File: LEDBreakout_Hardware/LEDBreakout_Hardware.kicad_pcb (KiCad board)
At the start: 2 copper layers, 42.7 x 25.9 mm, 19 parts

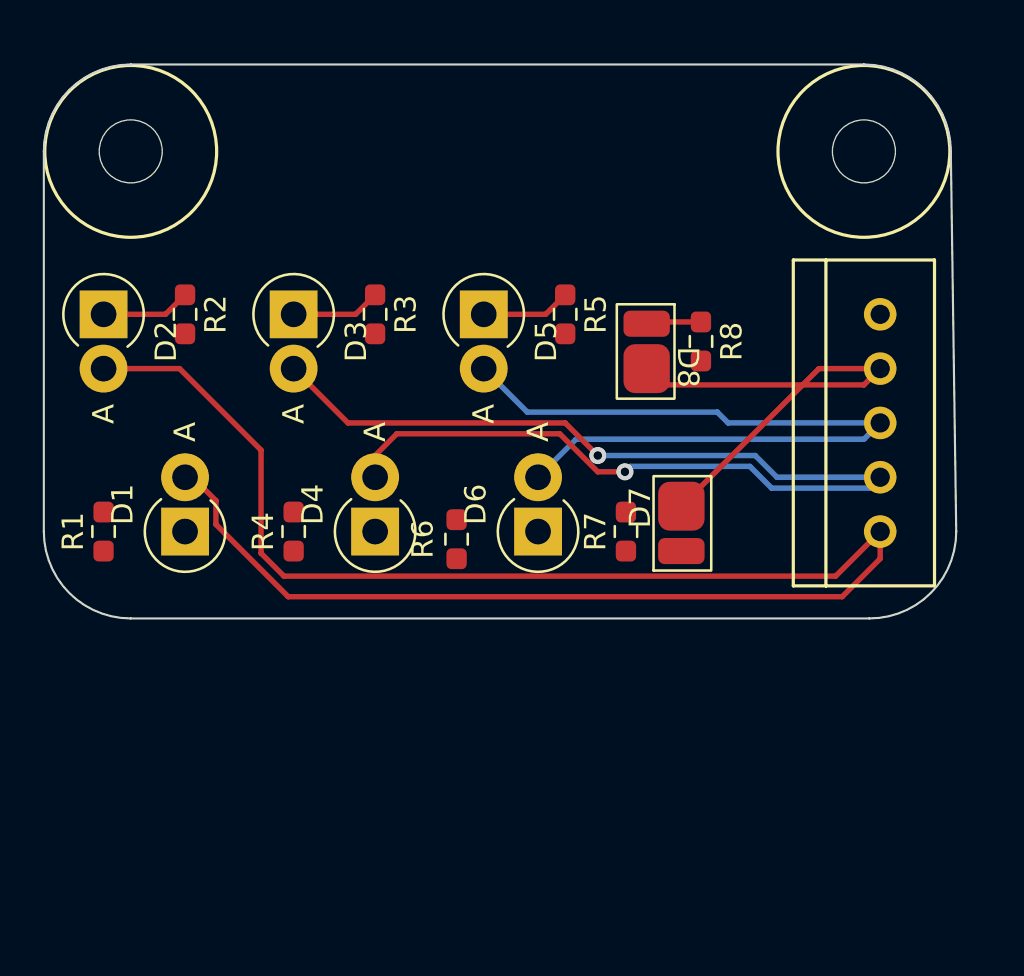
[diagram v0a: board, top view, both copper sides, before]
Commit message: Added 5V to LED connectors
Also added FETs to LEDs on breakout.
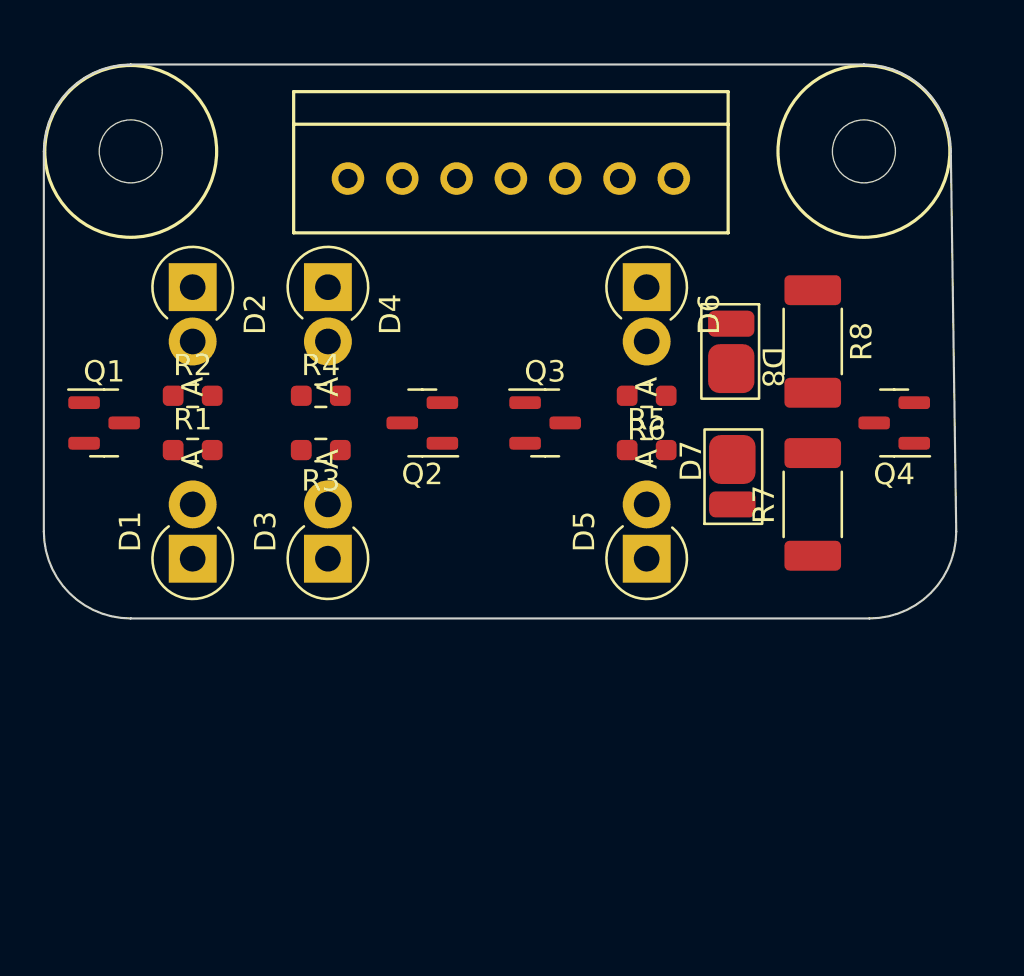
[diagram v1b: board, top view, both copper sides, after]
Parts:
- added Q1: BSS138, Package_TO_SOT_SMD:SOT-23, F.Cu at (64.8, 76.2)
- added Q2: BSS138, Package_TO_SOT_SMD:SOT-23, F.Cu at (79.7, 76.2)
- added Q3: BSS138, Package_TO_SOT_SMD:SOT-23, F.Cu at (85.4, 76.2)
- added Q4: BSS138, Package_TO_SOT_SMD:SOT-23, F.Cu at (101.7, 76.2)
- Conn1: value Molex_SL_05 -> Molex_SL_07; footprint MRDT_Connectors:MOLEX_SL_05_Vertical -> MRDT_Connectors:MOLEX_SL_07_Vertical
- R1, R2: value 90 Ω -> 88.7 Ω
- R3, R4: value 80 Ω -> 78.7 Ω
- R5, R6: value 57 Ω -> 82.5 Ω
- R7, R8: value 10 Ω -> 8 Ω; footprint Resistor_SMD:R_0603_1608Metric_Pad0.98x0.95mm_HandSolder -> Resistor_SMD:R_2010_5025Metric_Pad1.40x2.65mm_HandSolder
- moved Conn1 29.9 mm to (76.2, 64.8), turned to 0 degrees
- moved D5 13.7 mm to (90.2, 82.5), turned to 90 degrees
- moved D6 12.5 mm to (90.2, 69.8), turned to -90 degrees
- moved D4 11.6 mm to (75.3, 69.8), turned to -90 degrees
- moved D3 11.5 mm to (75.3, 82.5), turned to 90 degrees
- moved R6 11.1 mm to (90.2, 74.9), turned to 180 degrees
- moved R7 8.83 mm to (97.9, 80.0)
- moved R5 7.41 mm to (90.2, 77.5), turned to 0 degrees
- moved R3 6.84 mm to (74.9, 77.5), turned to 180 degrees
- moved R4 6.48 mm to (74.9, 74.9), turned to 0 degrees
- moved R1 5.65 mm to (68.9, 77.5), turned to 0 degrees
- moved R8 5.23 mm to (97.9, 72.4)
- moved D2 4.36 mm to (68.9, 69.8)
- moved D8 3.96 mm to (94.2, 72.5)
- moved R2 3.83 mm to (68.9, 74.9), turned to 0 degrees
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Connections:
- Conn1 pad 1: Net-(D1-A) -> 530nm
- Conn1 pad 2: Net-(D3-A) -> 522nm
- Conn1 pad 3: Net-(D5-A) -> 465nm
- Conn1 pad 4: Net-(D7-A) -> 400nm
- Conn1 pad 5: GND -> +5V
- D2 pad 1: Net-(D2-K) -> Net-(D1-K)
- D2 pad 2: Net-(D1-A) -> Net-(D2-A)
- D4 pad 1: Net-(D4-K) -> Net-(D3-K)
- D4 pad 2: Net-(D3-A) -> Net-(D4-A)
- D6 pad 1: Net-(D6-K) -> Net-(D5-K)
- D6 pad 2: Net-(D5-A) -> Net-(D6-A)
- D8 pad 1: Net-(D8-K) -> Net-(D7-K)
- D8 pad 2: Net-(D7-A) -> Net-(D8-A)
- R1 pad 1: Net-(D1-K) -> +5V
- R1 pad 2: GND -> Net-(D1-A)
- R2 pad 1: Net-(D2-K) -> +5V
- R2 pad 2: GND -> Net-(D2-A)
- R3 pad 1: Net-(D3-K) -> +5V
- R3 pad 2: GND -> Net-(D3-A)
- R4 pad 1: Net-(D4-K) -> +5V
- R4 pad 2: GND -> Net-(D4-A)
- R5 pad 1: Net-(D5-K) -> +5V
- R5 pad 2: GND -> Net-(D5-A)
- R6 pad 1: Net-(D6-K) -> +5V
- R6 pad 2: GND -> Net-(D6-A)
- R7 pad 1: Net-(D7-K) -> +5V
- R7 pad 2: GND -> Net-(D7-A)
- R8 pad 1: Net-(D8-K) -> +5V
- R8 pad 2: GND -> Net-(D8-A)
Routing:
- net Net-(D1-A): track 81.8 -> 0.00 mm
- net Net-(D3-A): track 56.1 -> 0.00 mm, vias 2 -> 0
- net Net-(D5-A): track 36.6 -> 0.00 mm
- net Net-(D7-A): track 23.5 -> 0.00 mm
- net Net-(D5-K): track 4.19 -> 0.00 mm
- net Net-(D3-K): track 4.19 -> 0.00 mm
- net Net-(D2-K): track 4.19 -> 0.00 mm
- net Net-(D8-K): track 2.57 -> 0.00 mm

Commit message: Added Traces for LED Breakout
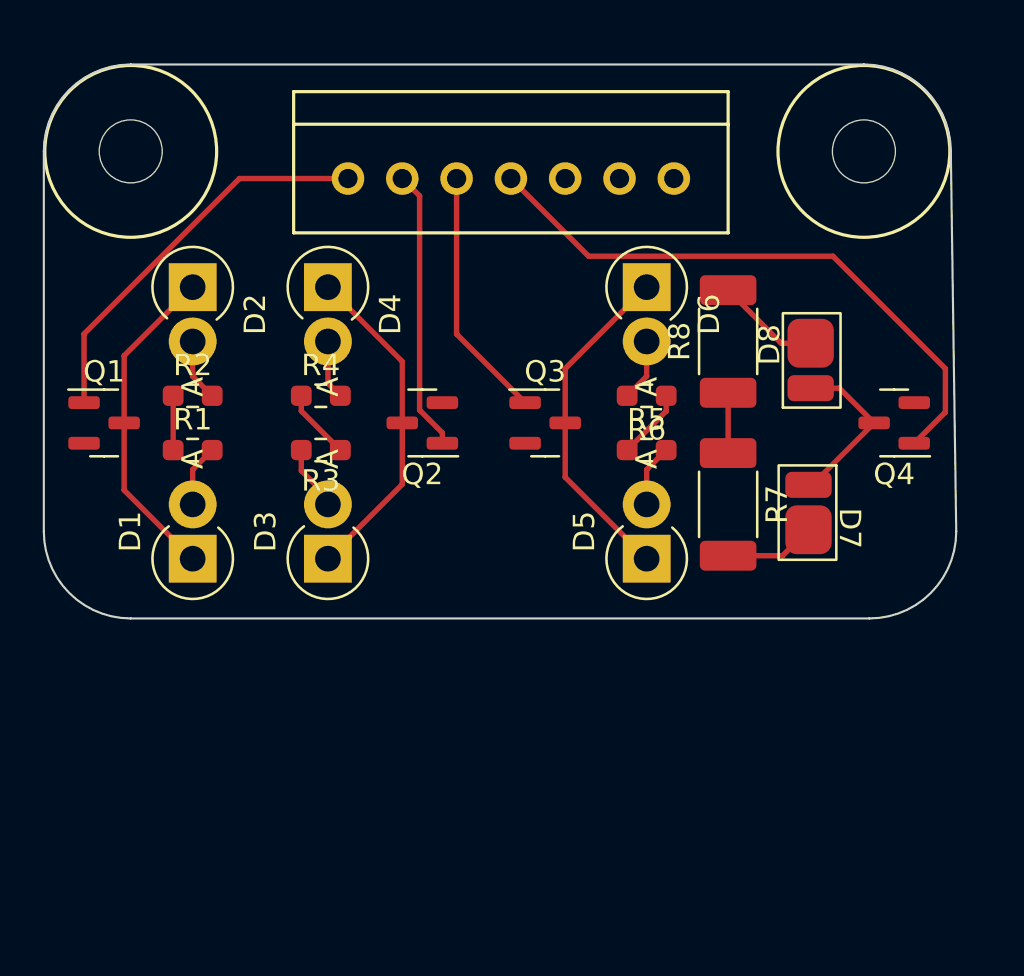
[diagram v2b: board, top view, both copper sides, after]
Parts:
- moved R7 3.96 mm to (94.0, 80.0), turned to -90 degrees
- moved R8 3.96 mm to (94.0, 72.4), turned to 90 degrees
- moved D8 3.80 mm to (97.8, 73.7), turned to 90 degrees
- moved D7 3.78 mm to (97.8, 80.0), turned to -90 degrees
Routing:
- net 400nm: track 0.00 -> 28.1 mm
- net 530nm: track 0.00 -> 18.6 mm
- net Net-(D3-K): track 0.00 -> 16.1 mm
- net Net-(D5-K): track 0.00 -> 15.9 mm
- net Net-(D1-K): track 0.00 -> 15.4 mm
- net 522nm: track 0.00 -> 13.2 mm
- net +5V: track 0.00 -> 12.0 mm
- net 465nm: track 0.00 -> 11.8 mm
- net Net-(D7-K): track 0.00 -> 7.91 mm
- net Net-(D8-A): track 0.00 -> 4.89 mm
- net Net-(D7-A): track 0.00 -> 4.26 mm
- net Net-(D3-A): track 0.00 -> 3.06 mm
- net Net-(D6-A): track 0.00 -> 2.92 mm
- net Net-(D5-A): track 0.00 -> 2.92 mm
- net Net-(D1-A): track 0.00 -> 2.92 mm
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
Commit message: Changes made based on layout review notes
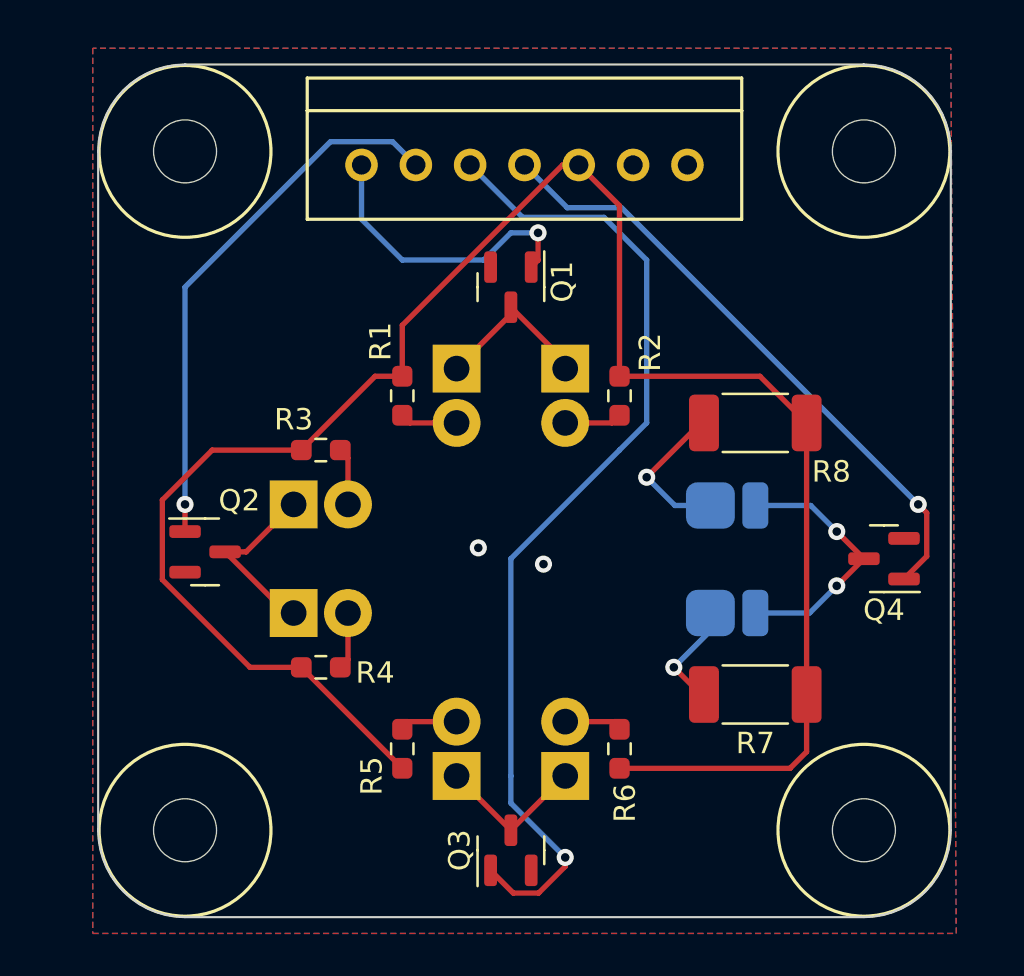
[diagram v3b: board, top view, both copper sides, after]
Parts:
- added REF**: 4_40_Hole, MRDT_Drill_Holes:4_40_Hole, F.Cu at (100.3, 95.2)
- added REF**: 4_40_Hole, MRDT_Drill_Holes:4_40_Hole, F.Cu at (68.6, 95.2)
- D1, D2, D3, D4, D5, D6, D7, D8: moved to B.Cu
- moved D6 23.2 mm to (86.4, 92.7), turned to 90 degrees
- moved Q1 20.1 mm to (83.8, 69.8), turned to -90 degrees
- moved Q3 20.1 mm to (83.8, 96.2), turned to 90 degrees
- moved R2 20.0 mm to (88.9, 74.9), turned to -90 degrees
- moved R5 18.1 mm to (78.7, 91.4), turned to 90 degrees
- moved D2 17.8 mm to (86.4, 73.7)
- moved R6 16.6 mm to (88.9, 91.4), turned to 90 degrees
- moved D4 15.3 mm to (73.7, 85.1), turned to 0 degrees
- moved D1 15.2 mm to (81.3, 73.7), turned to -90 degrees
- moved D5 13.5 mm to (81.3, 92.7)
- moved R4 12.7 mm to (74.9, 87.6)
- moved Q2 11.8 mm to (69.5, 82.2), turned to 0 degrees
- moved R1 10.1 mm to (78.7, 74.9), turned to -90 degrees
- moved R7 8.98 mm to (95.2, 88.9), turned to 180 degrees
- moved D8 7.23 mm to (94.3, 80.0), turned to 180 degrees
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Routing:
- net +5V: track 12.0 -> 90.7 mm
- net 465nm: track 11.8 -> 46.6 mm, vias 0 -> 1
- net 522nm: track 13.2 -> 25.5 mm, vias 0 -> 1
- net Net-(D5-K): track 15.9 -> 7.18 mm
- net Net-(D3-K): track 16.1 -> 8.51 mm
- net Net-(D1-K): track 15.4 -> 7.85 mm
- net 530nm: track 18.6 -> 13.8 mm, vias 0 -> 1
- net Net-(D7-K): track 7.91 -> 12.2 mm, vias 0 -> 2
- net Net-(D8-A): track 4.89 -> 7.26 mm, vias 0 -> 1
- net 400nm: track 28.1 -> 29.1 mm, vias 0 -> 1
- net Net-(D7-A): track 4.26 -> 5.18 mm, vias 0 -> 1
- net GND: vias 0 -> 2
- added copper zone on B.Cu, net GND
- added copper zone on F.Cu, net GND
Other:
- board size 42.7 x 25.9 mm -> 39.9 x 39.9 mm

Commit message: Added Pull Down Resistors to MOSFETs
And some other things
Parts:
- added R10: 4.7k Ω, Resistor_SMD:R_0603_1608Metric_Pad0.98x0.95mm_HandSolder, F.Cu at (67.8, 72.1)
- added R11: 4.7k Ω, Resistor_SMD:R_0603_1608Metric_Pad0.98x0.95mm_HandSolder, F.Cu at (67.8, 74.4)
- added R12: 4.7k Ω, Resistor_SMD:R_0603_1608Metric_Pad0.98x0.95mm_HandSolder, F.Cu at (67.8, 76.7)
- added R9: 4.7k Ω, Resistor_SMD:R_0603_1608Metric_Pad0.98x0.95mm_HandSolder, F.Cu at (67.8, 69.6)
- moved Q1 14.7 mm to (94.3, 80.2), turned to 180 degrees
- moved R1 10.5 mm to (89.1, 73.2), turned to 180 degrees
- moved Q4 6.59 mm to (96.5, 87.1)
- moved D3 6.12 mm to (79.8, 79.5), turned to 180 degrees
- moved R8 6.02 mm to (98.0, 81.5), turned to -90 degrees
- moved D2 5.99 mm to (89.9, 78.5), turned to 90 degrees
- moved D7 5.04 mm to (90.8, 88.6)
- moved D1 5.03 mm to (84.8, 77.2), turned to 90 degrees
- moved R2 4.75 mm to (93.5, 76.2), turned to 90 degrees
- moved Q2 4.66 mm to (73.5, 79.8), turned to -90 degrees
- moved D4 4.13 mm to (77.7, 84.3), turned to 180 degrees
- moved D5 3.78 mm to (80.0, 89.2), turned to -90 degrees
- moved D8 3.77 mm to (93.1, 83.6)
- moved R7 3.66 mm to (93.2, 91.9)
- moved R4 3.61 mm to (72.6, 84.8), turned to -90 degrees
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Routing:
- net +5V: track 90.7 -> 0.00 mm
- net 465nm: track 46.6 -> 0.00 mm, vias 1 -> 0
- net 400nm: track 29.1 -> 0.00 mm, vias 1 -> 0
- net 522nm: track 25.5 -> 0.00 mm, vias 1 -> 0
- net 530nm: track 13.8 -> 0.00 mm, vias 1 -> 0
- net Net-(D7-K): track 12.2 -> 0.00 mm, vias 2 -> 0
- net Net-(D3-K): track 8.51 -> 0.00 mm
- net Net-(D1-K): track 7.85 -> 0.00 mm
- net Net-(D8-A): track 7.26 -> 0.00 mm, vias 1 -> 0
- net Net-(D5-K): track 7.18 -> 0.00 mm
- net Net-(D7-A): track 5.18 -> 0.00 mm, vias 1 -> 0
- net Net-(D6-A): track 2.69 -> 0.00 mm
- net Net-(D5-A): track 2.69 -> 0.00 mm
- net Net-(D3-A): track 2.69 -> 0.00 mm
- net Net-(D2-A): track 2.69 -> 0.00 mm
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- added copper zone on F.Cu, net +5V
- removed copper zone on F.Cu, net GND
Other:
- board text added: "Fluorometer"
- board text added: "LED Breakout, Rev1 Mars Rover Design Team Missouri S&T, 2024 Ethan Williams, Tri Le"

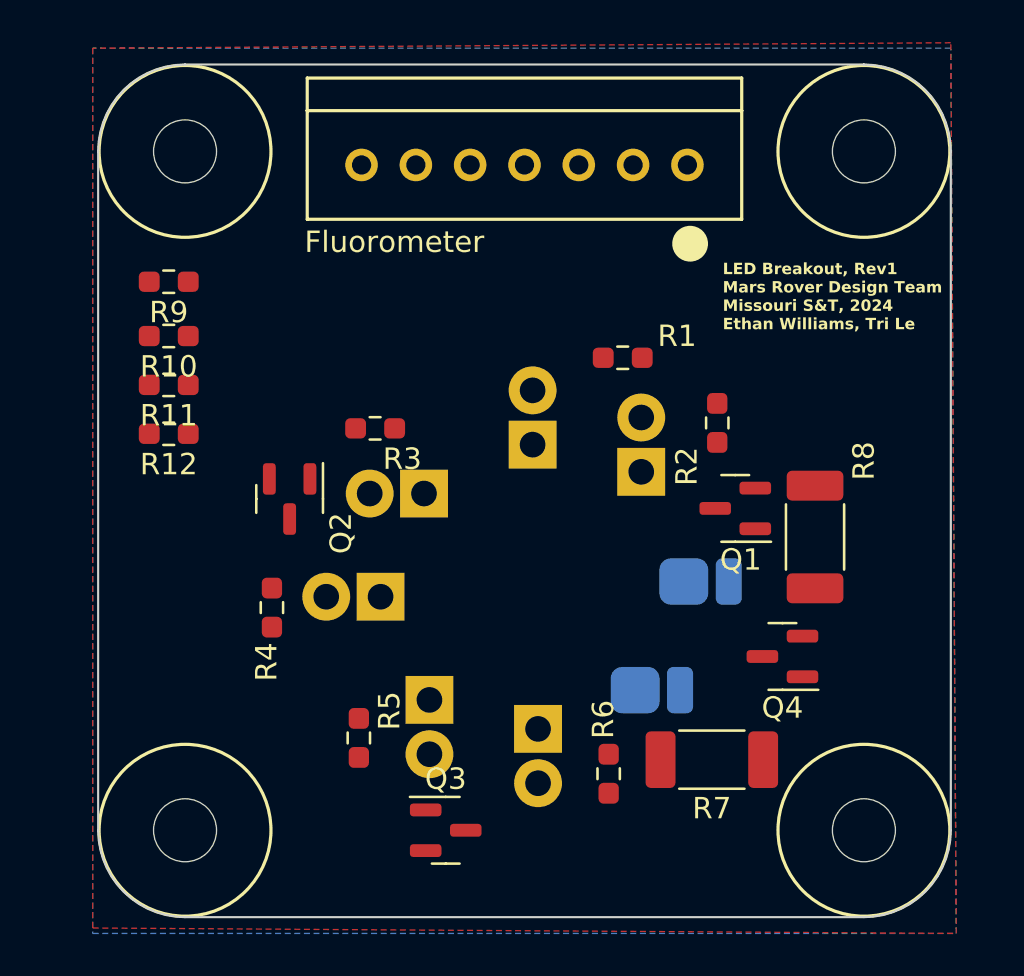
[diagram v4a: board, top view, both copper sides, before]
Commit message: Finished LED Breakout
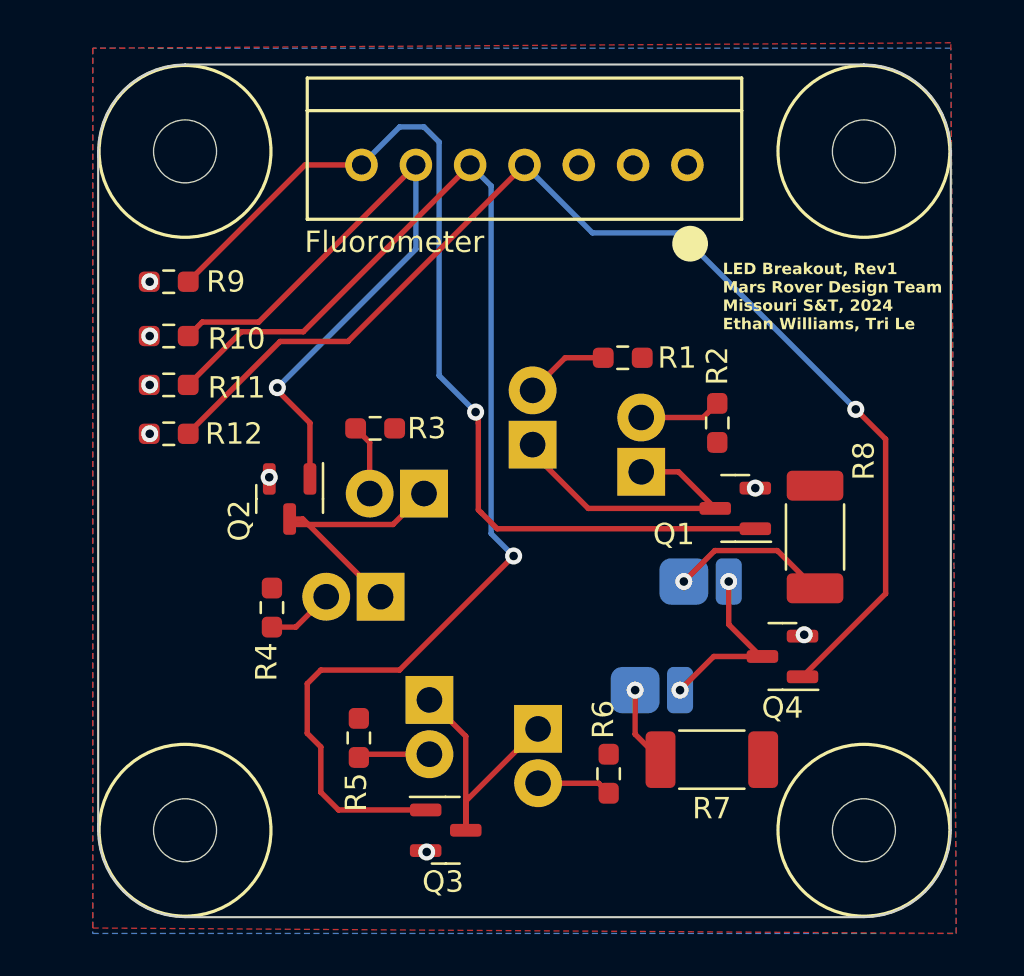
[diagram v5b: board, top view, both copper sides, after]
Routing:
- net 465nm: track 0.00 -> 59.3 mm, vias 0 -> 1
- net 400nm: track 0.00 -> 56.1 mm, vias 0 -> 1
- net 530nm: track 0.00 -> 46.3 mm, vias 0 -> 1
- net 522nm: track 0.00 -> 32.3 mm, vias 0 -> 1
- net Net-(D1-K): track 0.00 -> 14.2 mm
- net Net-(D5-K): track 0.00 -> 12.9 mm
- net Net-(D3-K): track 0.00 -> 12.7 mm
- net Net-(D7-K): track 0.00 -> 8.71 mm, vias 0 -> 2
- net Net-(D8-A): track 0.00 -> 7.76 mm, vias 0 -> 1
- net Net-(D1-A): track 0.00 -> 3.93 mm
- net Net-(D2-A): track 0.00 -> 3.83 mm
- net Net-(D7-A): track 0.00 -> 3.74 mm, vias 0 -> 1
- net Net-(D6-A): track 0.00 -> 3.50 mm
- net Net-(D5-A): track 0.00 -> 3.36 mm
- net Net-(D3-A): track 0.00 -> 3.32 mm
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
